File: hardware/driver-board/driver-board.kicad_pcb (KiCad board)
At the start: 4 copper layers, 111.8 x 69.8 mm, 72 parts, among them J1 Conn_ARM_JTAG_SWD_10, J2 USB_C_Receptacle_USB2.0_16P, J3 CONN_MOTOR_R, J4 CONN_MOTOR_L, Q1 AO3401A, Q2 AO4407A, SW1 SW_Push, SW2 SK-3296S-01-L2, U1 STM32F103CBT6, U2 USBLC6-2SC6, U3 DRV8838, U4 DRV8838, U5 LMR51430XDDCR, Y1 16Mhz

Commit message: Update driver board USB-C and power circuitry
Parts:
- removed L2: 39n, Inductor_SMD:L_0402_1005Metric
- removed R8, R9: 22, Resistor_SMD:R_0402_1005Metric
- C9: value 10u -> 100n; footprint Capacitor_SMD:C_0805_2012Metric -> Capacitor_SMD:C_0402_1005Metric
- J2: footprint Connector_USB:USB_C_Receptacle_G-Switch_GT-USB-7025 -> Connector_USB:USB_C_Receptacle_G-Switch_GT-USB-7010ASV
- moved R5 3.94 mm to (100.6, 119.5), turned to 0 degrees
- moved C9 2.74 mm to (97.0, 130.4), turned to 0 degrees
- moved U2 1.22 mm to (100.5, 129.9)
- moved J2 0.88 mm to (100.0, 138.1)
- moved R6 0.88 mm to (97.0, 131.6)
- moved R7 0.88 mm to (103.0, 131.6)
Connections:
- C22 pad 1: +3V3A -> +3V3
- C23 pad 1: +3V3A -> +3V3
- C9 pad 1: GND -> VBUS
- C9 pad 2: VBUS -> GND
- U1 pad 9: +3V3A -> +3V3
- U2 pad 1: /USB_CONN_D+ -> /USB_CONN_D-
- U2 pad 3: /USB_CONN_D- -> /USB_CONN_D+
- U2 pad 4: Net-(R9-Pad1) -> /USB_D+
- U2 pad 6: Net-(R8-Pad1) -> /USB_D-
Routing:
- net /USB_CONN_D+: track 0.00 -> 6.28 mm
- net /USB_CONN_D-: track 0.00 -> 5.47 mm
- net /Motor Control/ML-: track 0.00 -> 4.04 mm
- net /Motor Control/ML+: track 0.00 -> 3.88 mm
- net +3V3: track 7.64 -> 11.0 mm, vias 0 -> 4
- net GND: track 16.6 -> 19.9 mm, vias 13 -> 15
- net +3V3A: track 1.93 -> 0.00 mm
- net VBAT_SW: vias 0 -> 2
- added copper zone on In2.Cu, net +3V3
- added copper zone on In2.Cu, net VBAT_SW
- removed copper zone on F.Cu, net +3V3A

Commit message: Refine driver board layout and 3D models
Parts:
- moved D1 26.9 mm to (59.5, 120.0)
- moved R20 25.6 mm to (57.5, 120.0)
- moved R1 23.7 mm to (108.0, 111.0)
- moved D2 16.6 mm to (130.0, 136.0)
- moved C3 15.9 mm to (137.0, 136.0)
- moved SW1 15.9 mm to (134.0, 136.0)
- moved J1 12.5 mm to (124.0, 136.0), turned to 90 degrees
- moved R17 12.2 mm to (83.0, 120.2)
- moved R16 11.1 mm to (83.0, 121.5), turned to 0 degrees
- moved TP3 11.0 mm to (46.4, 122.0)
- moved R21 7.28 mm to (130.0, 127.0)
- moved R7 6.70 mm to (106.7, 137.2), turned to 90 degrees
- moved F1 6.27 mm to (54.0, 127.0), turned to 0 degrees
- moved R6 6.19 mm to (94.3, 137.2), turned to 90 degrees
- moved Q1 5.71 mm to (60.0, 129.0)
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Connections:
- U1 pad 26: DRV_R_PH -> DRV_L_SLEEP_N
- U1 pad 27: DRV_L_SLEEP_N -> DRV_R_PH
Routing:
- net /Power/BT2+: track 1.52 -> 34.2 mm
- net /USB_D-: track 0.00 -> 15.4 mm
- net /USB_D+: track 0.00 -> 15.4 mm
- net VBUS: track 0.00 -> 15.1 mm
- net /Power/REG_SW: track 0.00 -> 11.3 mm, vias 0 -> 2
- net /Power/VBAT_SAFE: track 0.00 -> 9.66 mm
- net GND: track 19.9 -> 29.1 mm, vias 15 -> 39
- net +3V3: track 11.0 -> 19.0 mm, vias 4 -> 15
- net Net-(J2-CC1): track 0.00 -> 6.50 mm
- net VBAT_SW: track 0.00 -> 6.35 mm, vias 2 -> 12
- net Net-(J2-CC2): track 0.00 -> 6.24 mm
- net Net-(Q2-G): track 0.00 -> 5.03 mm
- net VBAT: track 0.00 -> 4.98 mm
- net Net-(U5-FB): track 0.00 -> 3.68 mm
- net Net-(SW2-B): track 0.00 -> 2.35 mm
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- added copper zone on F.Cu, net /Power/VBAT_FUSED
- added copper zone on F.Cu, net /Power/VBAT_SAFE
- added copper zone on F.Cu, net VBAT

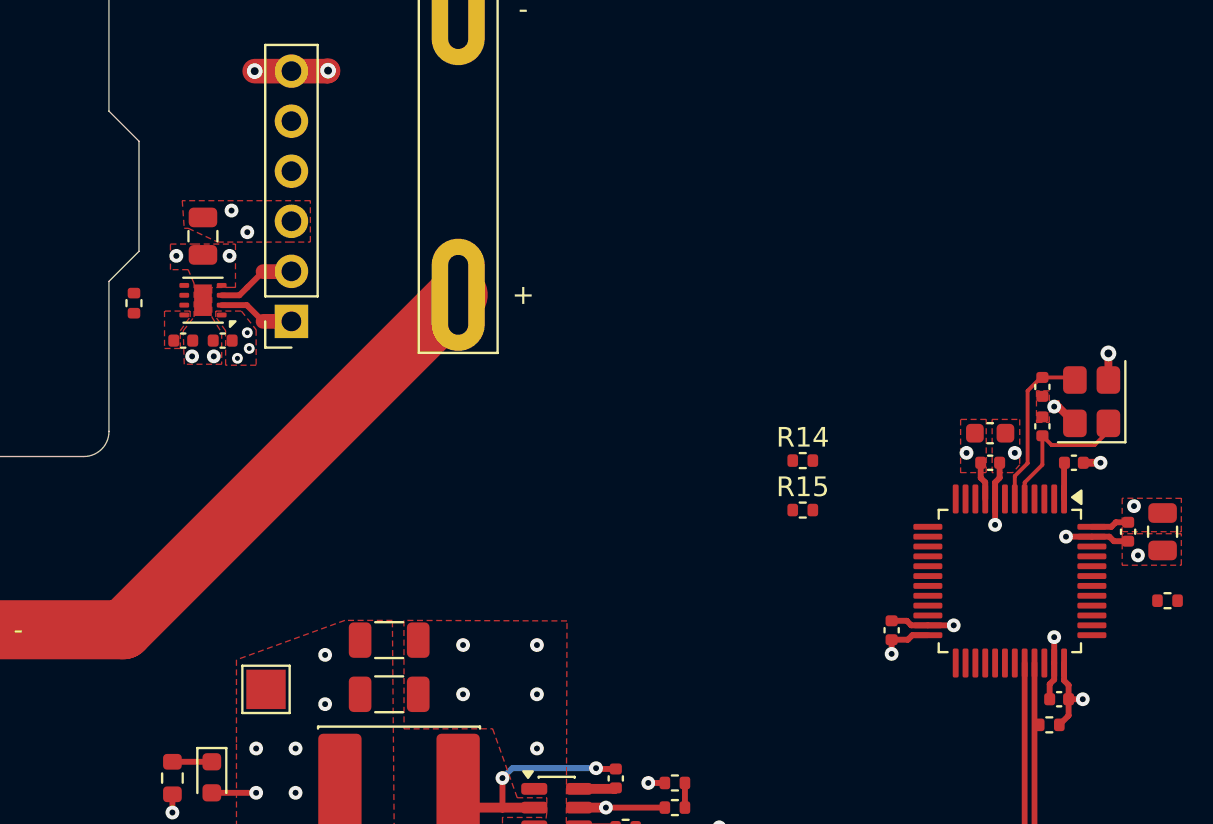
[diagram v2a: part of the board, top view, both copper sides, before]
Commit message: Checkpoint left motor driver layout
Capture the routed left motor-driver state before relocation, align the STM32 IOC labels with the schematic pin mapping, and save the current Rev A purchasing and Rev B planning notes.
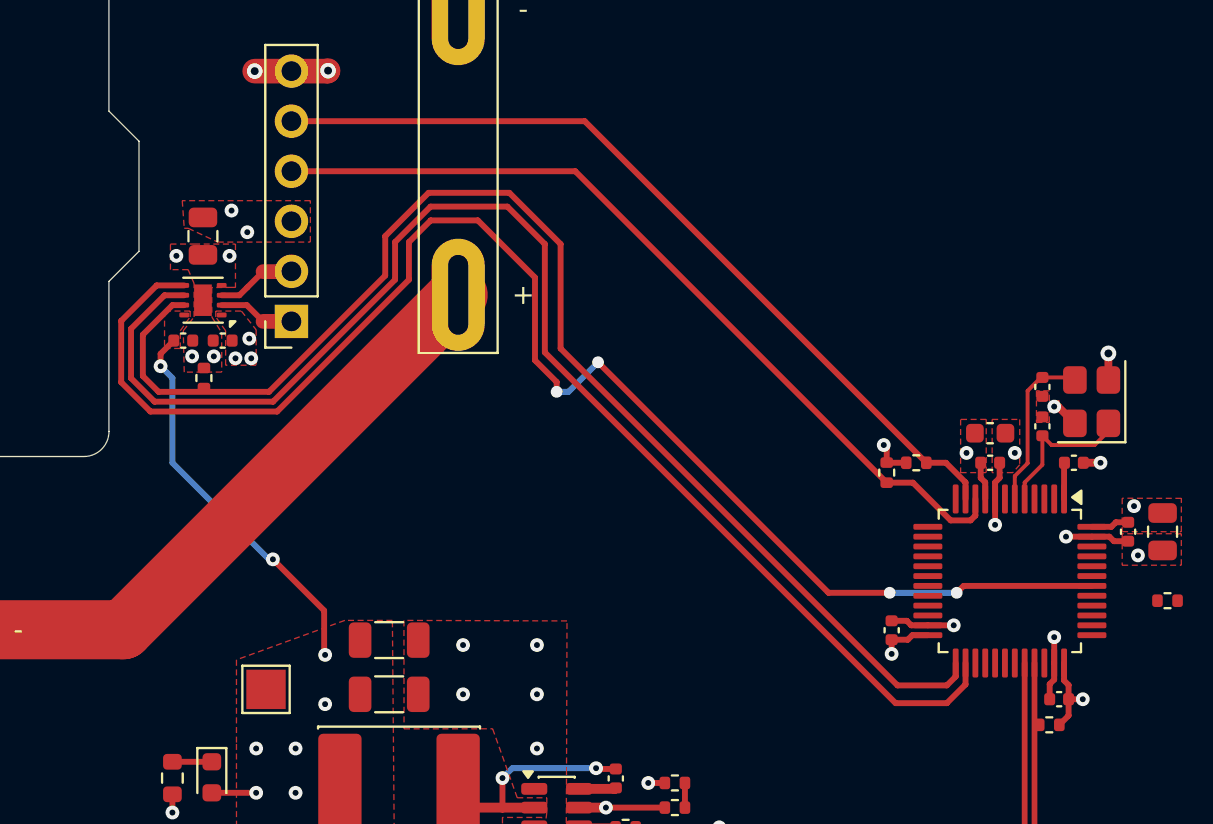
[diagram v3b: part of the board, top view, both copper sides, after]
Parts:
- moved R14 5.76 mm to (95.2, 104.0)
- moved R12 5.20 mm to (59.1, 99.7), turned to -90 degrees
- moved R15 4.66 mm to (93.8, 104.5), turned to -90 degrees
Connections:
- U1 pad 10: ENC_L_A -> ENC_L_B
- U1 pad 11: ENC_L_B -> ENC_L_A
- U1 pad 25: DRV_L_PH -> DRV_L_SLEEP_N
- U1 pad 26: DRV_L_SLEEP_N -> DRV_L_PH
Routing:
- net DRV_L_EN: track 0.00 -> 74.0 mm, vias 0 -> 4
- net DRV_L_PH: track 0.00 -> 69.1 mm
- net DRV_L_SLEEP_N: track 0.00 -> 66.1 mm
- net ENC_L_B: track 0.00 -> 43.0 mm
- net ENC_L_A: track 0.00 -> 42.6 mm
- net +3V3: track 19.0 -> 40.8 mm, vias 15 -> 18

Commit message: Checkpoint left driver and firmware pin mapping
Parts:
- moved R12 19.3 mm to (78.2, 97.0), turned to 180 degrees
- moved C12 11.0 mm to (68.2, 93.8), turned to 180 degrees
- moved U3 8.15 mm to (67.2, 95.8), turned to 0 degrees
- moved C10 8.02 mm to (67.0, 92.0), turned to 0 degrees
- moved C11 7.41 mm to (66.2, 93.8), turned to 0 degrees
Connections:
- J4 pad 1: /Motor Control/ML+ -> /Motor Control/ML-
- J4 pad 2: /Motor Control/ML- -> /Motor Control/ML+
- U1 pad 27: DRV_R_PH -> DRV_L_EN
- U1 pad 42: DRV_L_EN -> DRV_R_PH
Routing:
- net DRV_L_EN: track 74.0 -> 43.3 mm, vias 4 -> 2
- net DRV_L_PH: track 69.1 -> 45.9 mm
- net DRV_L_SLEEP_N: track 66.1 -> 44.9 mm
- net VBAT_SW: track 6.35 -> 12.3 mm, vias 12 -> 9
- net /Power/BT2+: track 34.2 -> 38.1 mm
- net +3V3: track 40.8 -> 44.4 mm, vias 18 -> 17
- net /Motor Control/ML-: track 4.04 -> 3.05 mm
- net GND: track 29.1 -> 30.1 mm, vias 39 -> 42
- net /Motor Control/ML+: track 3.88 -> 3.38 mm

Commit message: Complete motor driver layouts and pin mapping
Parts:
- moved R13 13.8 mm to (129.6, 89.2), turned to 180 degrees
- moved C15 10.8 mm to (131.5, 87.5)
- moved R10 10.1 mm to (110.8, 112.2)
- moved R11 8.16 mm to (109.8, 113.2), turned to -90 degrees
- moved C13 8.00 mm to (132.5, 89.2), turned to 180 degrees
- moved U4 8.00 mm to (132.5, 85.5), turned to 180 degrees
- moved C14 7.23 mm to (133.5, 87.5), turned to 180 degrees
- moved R1 6.39 mm to (104.8, 105.5), turned to -90 degrees
- moved R14 4.83 mm to (93.5, 108.5)
- moved R15 4.83 mm to (92.0, 109.0)
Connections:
- J1 pad 6: /SWO -> unconnected-(J1-SWO/TDO-Pad6)
- J3 pad 5: /Motor Control/MR- -> /Motor Control/MR+
- J3 pad 6: /Motor Control/MR+ -> /Motor Control/MR-
- U1 pad 10: ENC_L_B -> unconnected-(U1-PA0-Pad10)
- U1 pad 11: ENC_L_A -> unconnected-(U1-PA1-Pad11)
- U1 pad 16: ENC_R_A -> ENC_L_A
- U1 pad 17: ENC_R_B -> ENC_L_B
- U1 pad 28: DRV_R_SLEEP_N -> unconnected-(U1-PB15-Pad28)
- U1 pad 38: unconnected-(U1-PA15-Pad38) -> ENC_R_B
- U1 pad 39: /SWO -> ENC_R_A
- U1 pad 41: unconnected-(U1-PB5-Pad41) -> DRV_R_SLEEP_N
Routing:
- net ENC_R_B: track 0.00 -> 41.0 mm
- net DRV_R_SLEEP_N: track 0.00 -> 40.8 mm
- net ENC_R_A: track 0.00 -> 40.6 mm
- net DRV_R_PH: track 0.00 -> 40.3 mm
- net DRV_R_EN: track 0.00 -> 40.2 mm
- net +3V3: track 44.4 -> 68.1 mm, vias 17 -> 21
- net BATLEV: track 1.25 -> 18.1 mm, vias 0 -> 2
- net VBAT_SW: track 12.3 -> 18.7 mm, vias 9 -> 11
- net /BOOT0: track 0.00 -> 6.32 mm
- net GND: track 30.1 -> 34.5 mm, vias 42 -> 51
- net /Motor Control/MR-: track 0.00 -> 3.48 mm
- net /Motor Control/MR+: track 0.00 -> 3.39 mm
- net ENC_L_A: track 42.6 -> 45.1 mm
- net ENC_L_B: track 43.0 -> 44.6 mm

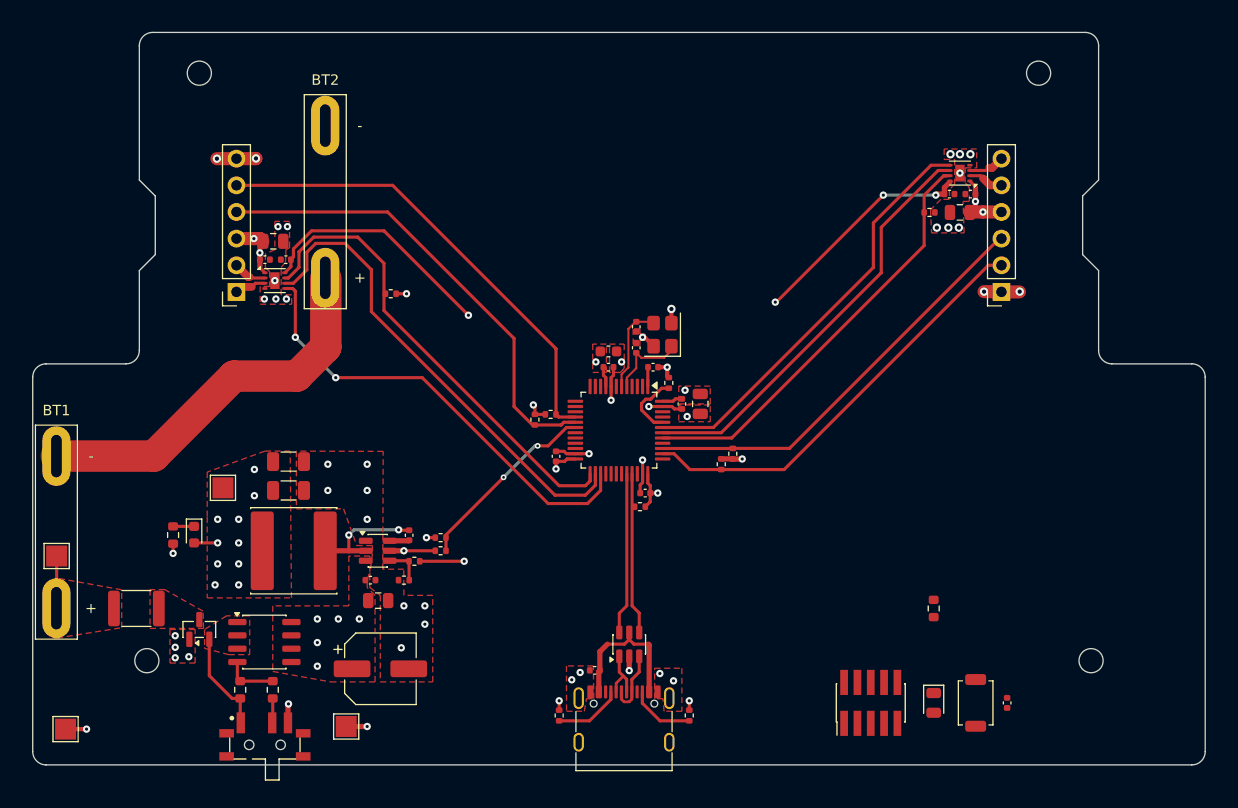
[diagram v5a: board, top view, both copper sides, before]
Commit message: Checkpoint status LED move to PB4
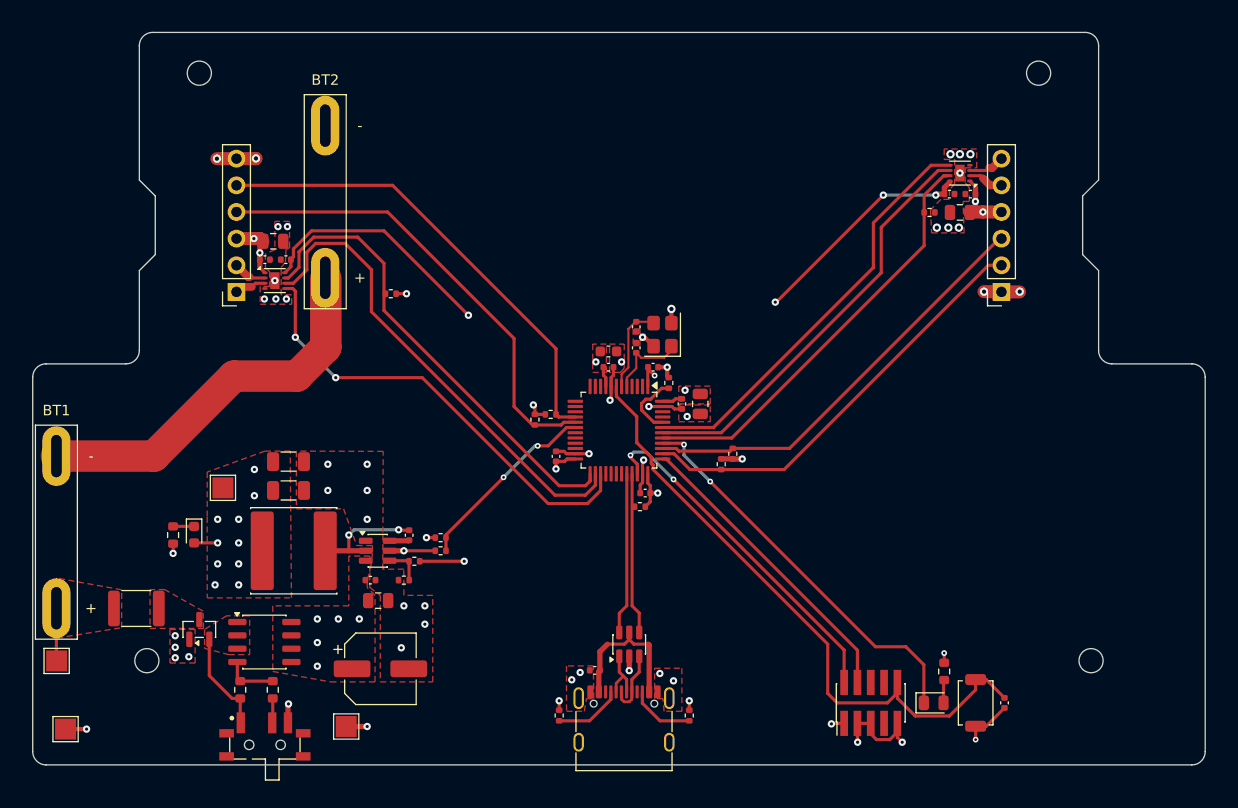
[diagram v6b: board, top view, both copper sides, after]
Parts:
- moved TP3 10.0 mm to (46.4, 132.0)
- moved R21 6.08 mm to (131.0, 133.0)
- moved C3 0.25 mm to (136.8, 136.0)
- turned D2 to 0 degrees
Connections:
- U1 pad 2: Net-(D2-K) -> unconnected-(U1-PC13-Pad2)
- U1 pad 40: unconnected-(U1-PB4-Pad40) -> Net-(D2-K)
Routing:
- net /NRST: track 0.00 -> 61.2 mm
- net Net-(D2-K): track 0.00 -> 37.9 mm, vias 0 -> 2
- net /SWDIO: track 0.00 -> 33.4 mm, vias 0 -> 2
- net /SWCLK: track 0.00 -> 29.2 mm
- net GND: track 34.5 -> 49.2 mm, vias 51 -> 54
- net +3V3: track 68.1 -> 71.3 mm, vias 21 -> 24
- net Net-(D2-A): track 0.00 -> 2.20 mm

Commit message: Finalize Rev A PCB and hardware docs
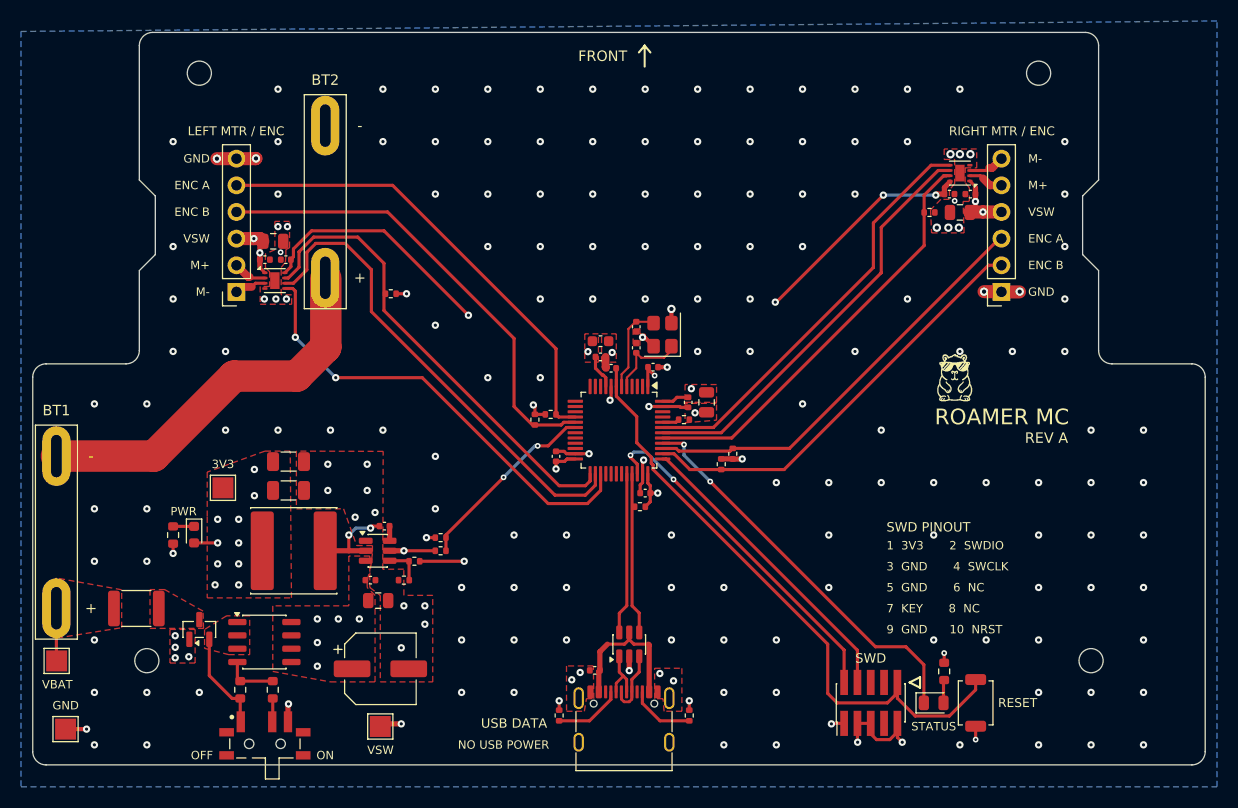
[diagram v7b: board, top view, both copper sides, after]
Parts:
- added G1: CAPYBARA_ARTWORK, Capybara_Sunglasses, F.Cu at (132.0, 96.0)
- moved C3 49.2 mm to (99.2, 104.1), turned to 0 degrees
- moved R1 3.79 mm to (106.2, 109.0), turned to 180 degrees
- moved TP4 3.25 mm to (77.2, 138.2)
- moved C19 2.51 mm to (77.7, 119.2), turned to 180 degrees
- moved C22 1.24 mm to (98.2, 103.0)
- moved C23 1.24 mm to (98.2, 101.5)
- moved C7 0.62 mm to (106.6, 107.3)
- moved C8 0.62 mm to (108.3, 107.3)
- moved SW2 0.10 mm to (66.2, 139.9)
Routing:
- net GND: track 49.2 -> 44.3 mm, vias 54 -> 191
- net /BOOT0: track 6.32 -> 1.63 mm
- net /Power/REG_SW: track 11.3 -> 8.63 mm
- net +3V3: track 71.3 -> 73.4 mm
- net /NRST: track 61.2 -> 59.5 mm
- added copper zone on B.Cu, net GND
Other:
- board text added: "1 3V3 2 SWDIO"
- board text added: "3 GND 4 SWCLK"
- board text added: "3V3"
- board text added: "5 GND 6 NC"
- board text added: "7 KEY 8 NC"
- board text added: "9 GND 10 NRST"
- board text added: "ENC A"
- board text added: "ENC B"
- board text added: "FRONT"
- board text added: "GND"
- board text added: "LEFT MTR / ENC"
- board text added: "M+"
- board text added: "M-"
- board text added: "NO USB POWER"
- board text added: "OFF"
- board text added: "ON"
- board text added: "PWR"
- board text added: "RESET"
- board text added: "REV A"
- board text added: "RIGHT MTR / ENC"
- board text added: "ROAMER MC"
- board text added: "STATUS"
- board text added: "SWD"
- board text added: "SWD PINOUT"
- board text added: "USB DATA"
- board text added: "VBAT"
- board text added: "VSW"
